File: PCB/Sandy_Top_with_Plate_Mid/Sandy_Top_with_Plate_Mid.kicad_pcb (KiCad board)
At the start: 2 copper layers, 285 x 75.1 mm, 63 parts, among them J1 Conn_02x02_Top_Bottom, J2 Conn_02x02_Top_Bottom, J3 Conn_02x02_Top_Bottom

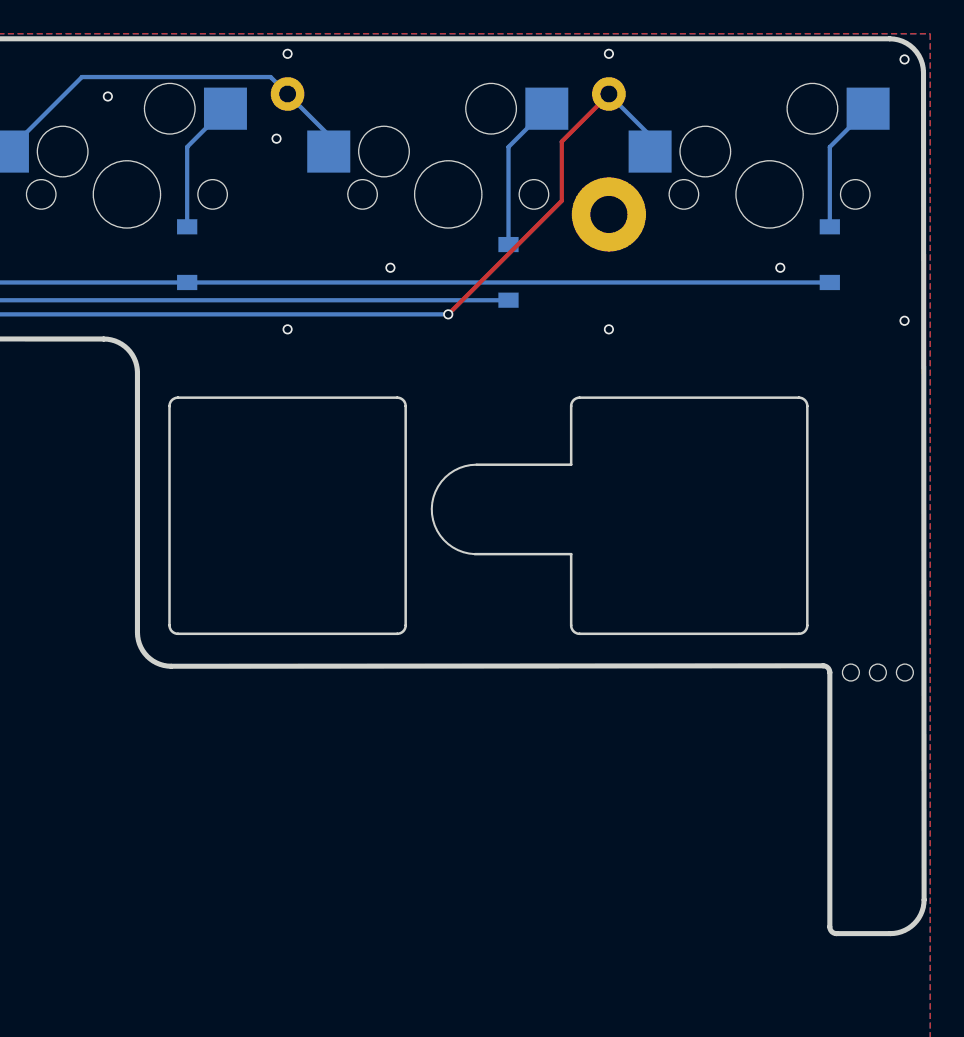
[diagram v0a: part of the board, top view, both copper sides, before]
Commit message: バージョン表記部分にプレートである旨を追記
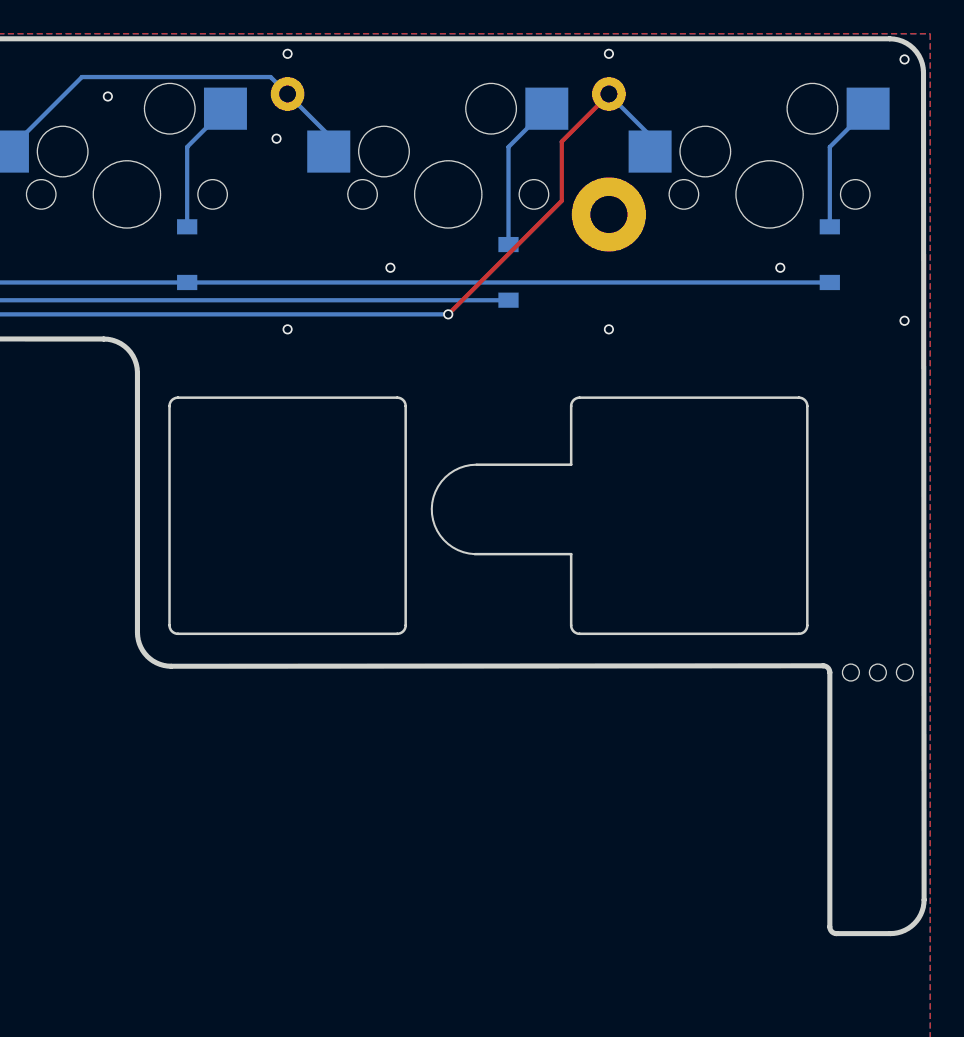
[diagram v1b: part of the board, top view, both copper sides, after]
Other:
- board text added: "#Sandy_kbd v.0.2 Top & Mid plate by @jpskenn"
- board text removed: "#Sandy_kbd v.0.2, Top by @jpskenn"
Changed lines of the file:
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@@
     (fp_arc (start -118.325 -37.80004) (mid -118.678553 -37.946487) (end -118.825 -38.30004)
       (stroke (width 0.1) (type solid)) (layer "Dwgs.User"))
-    (fp_arc (start 114.175 -9.90004) (mid 114.731476 -11.243582) (end 116.075 -11.80004)
+    (fp_arc (start 114.175 -9.90004) (mid 114.731482 -11.243546) (end 116.075 -11.80004)
       (stroke (width 0.12) (type solid)) (layer "Dwgs.User"))
-    (fp_arc (start 114.923491 -9.898554) (mid 115.274975 -10.747086) (end 116.123491 -11.098554)
+    (fp_arc (start 114.923491 -9.898554) (mid 115.274981 -10.74705) (end 116.123491 -11.098554)
       (stroke (width 0.12) (type solid)) (layer "Dwgs.User"))
-    (fp_arc (start 116.075 -8.00004) (mid 114.731482 -8.55651) (end 114.175 -9.90004)
+    (fp_arc (start 116.075 -8.00004) (mid 114.731447 -8.556504) (end 114.175 -9.90004)
       (stroke (width 0.12) (type solid)) (layer "Dwgs.User"))
-    (fp_arc (start 116.123491 -8.698554) (mid 115.274982 -9.050056) (end 114.923491 -9.898554)
+    (fp_arc (start 116.123491 -8.698554) (mid 115.275017 -9.050062) (end 114.923491 -9.898554)
       (stroke (width 0.12) (type solid)) (layer "Dwgs.User"))
-    (fp_arc (start 118.923491 -11.098554) (mid 119.772038 -10.747112) (end 120.123491 -9.898554)
+    (fp_arc (start 118.923491 -11.098554) (mid 119.772073 -10.747118) (end 120.123491 -9.898554)
       (stroke (width 0.12) (type solid)) (layer "Dwgs.User"))
-    (fp_arc (start 118.975 -11.80004) (mid 120.318488 -11.243516) (end 120.875 -9.90004)
+    (fp_arc (start 118.975 -11.80004) (mid 120.318452 -11.24351) (end 120.875 -9.90004)
       (stroke (width 0.12) (type solid)) (layer "Dwgs.User"))
-    (fp_arc (start 120.123491 -9.898554) (mid 119.772032 -9.050029) (end 118.923491 -8.698554)
+    (fp_arc (start 120.123491 -9.898554) (mid 119.772038 -9.049994) (end 118.923491 -8.698554)
       (stroke (width 0.12) (type solid)) (layer "Dwgs.User"))
-    (fp_arc (start 120.875 -9.90004) (mid 120.318482 -8.556576) (end 118.975 -8.00004)
+    (fp_arc (start 120.875 -9.90004) (mid 120.318488 -8.556541) (end 118.975 -8.00004)
       (stroke (width 0.12) (type solid)) (layer "Dwgs.User"))
     (fp_circle (center -117.325 -9.90004) (end -116.025 -9.90004)
@@
     (fp_arc (start 27.975 20.214174) (mid 28.560766 18.799948) (end 29.975 18.214174)
       (stroke (width 0.3) (type solid)) (layer "Edge.Cuts"))
-    (fp_arc (start 27.975 35.345746) (mid 27.389238 36.759982) (end 25.975 37.345746)
+    (fp_arc (start 27.975 35.345746) (mid 27.389238 36.759986) (end 25.975 37.345746)
       (stroke (width 0.3) (type solid)) (layer "Edge.Cuts"))
     (fp_arc (start 35.075 2.525) (mid 35.428553 2.671447) (end 35.575 3.025)
@@
     (fp_arc (start 56.555 -2.937398) (mid 55.969213 -1.523186) (end 54.555 -0.937398)
       (stroke (width 0.3) (type solid)) (layer "Edge.Cuts"))
-    (fp_arc (start 93.875 -20.001612) (mid 95.289212 -19.41585) (end 95.875 -18.001612)
+    (fp_arc (start 93.875 -20.001612) (mid 95.289182 -19.41582) (end 95.875 -18.001612)
       (stroke (width 0.3) (type solid)) (layer "Edge.Cuts"))
     (fp_arc (start 97.775 -16.025) (mid 97.921447 -16.378553) (end 98.275 -16.525)
       (stroke (width 0.15) (type solid)) (layer "Edge.Cuts"))
-    (fp_arc (start 97.875 -0.60004) (mid 96.460771 -1.1858) (end 95.875 -2.60004)
+    (fp_arc (start 97.875 -0.60004) (mid 96.460736 -1.185794) (end 95.875 -2.60004)
       (stroke (width 0.3) (type solid)) (layer "Edge.Cuts"))
     (fp_arc (start 98.275 -2.525) (mid 97.921447 -2.671447) (end 97.775 -3.025)
@@
     (fp_arc (start 136.521875 -0.628468) (mid 136.804693 -0.511288) (end 136.921875 -0.228468)
       (stroke (width 0.3) (type solid)) (layer "Edge.Cuts"))
-    (fp_arc (start 137.321875 15.249657) (mid 137.039034 15.132518) (end 136.921875 14.849657)
+    (fp_arc (start 137.321875 15.249657) (mid 137.038999 15.132524) (end 136.921875 14.849657)
       (stroke (width 0.3) (type solid)) (layer "Edge.Cuts"))
-    (fp_arc (start 140.475 -37.80004) (mid 141.889198 -37.214227) (end 142.475 -35.80004)
+    (fp_arc (start 140.475 -37.80004) (mid 141.889163 -37.214221) (end 142.475 -35.80004)
       (stroke (width 0.3) (type solid)) (layer "Edge.Cuts"))
     (fp_arc (start 142.510786 13.249657) (mid 141.925014 14.663893) (end 140.510786 15.249657)
@@
     (effects (font (size 2.5 2.5) (thickness 0.4) italic) (justify mirror))
   )
-  (gr_text "#Sandy_kbd v.0.2, Top\nby @jpskenn" (at 169 51.7) (layer "B.SilkS")
+  (gr_text "#Sandy_kbd v.0.2\nTop & Mid plate\nby @jpskenn" (at 166.314685 53.197155) (layer "B.SilkS")
     (effects (font (size 1.6 1.6) (thickness 0.15)) (justify left mirror))
   )

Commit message: Top基板（Midプレート付き）からディフューザーを削除
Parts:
- REF**: footprint locallib:60_Outline-Sandy-Top2-with-Mid-plate-from-Mid4 -> locallib:60_Outline-Sandy-Top3-with-Mid-plate-from-Mid4
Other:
- outline, holes or cut-outs redrawn

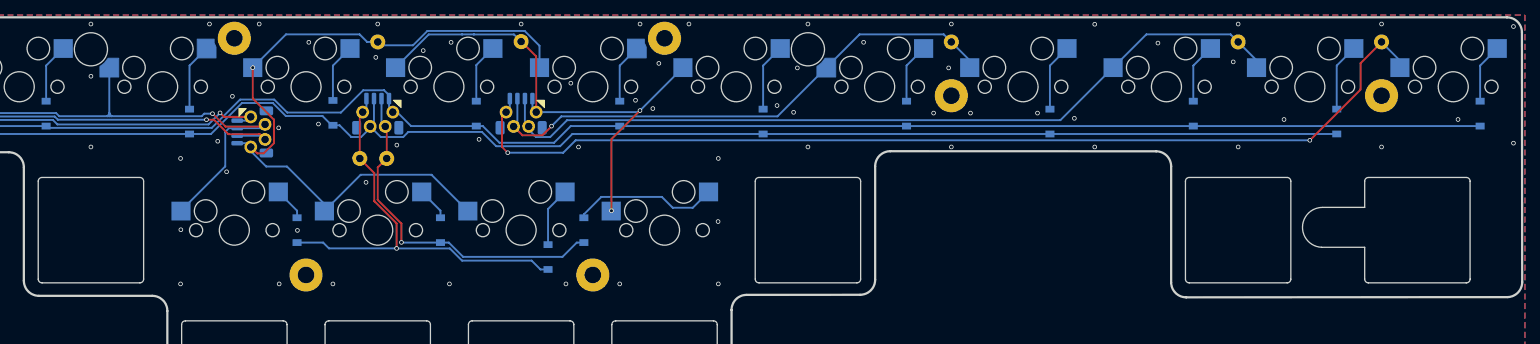
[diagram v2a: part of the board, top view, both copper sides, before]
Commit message: ソケットに近いSHコネクタ2個を少し後ろに下げ、ケーブルを抜き差ししやすくした
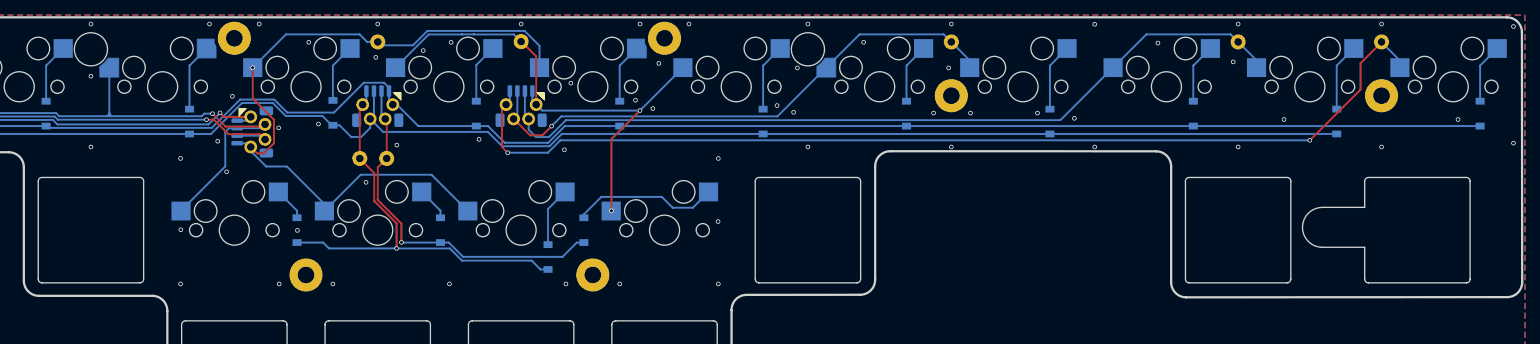
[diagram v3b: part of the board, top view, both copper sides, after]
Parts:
- moved J1 1.00 mm to (167.5, 29.6)
- moved J2 1.00 mm to (148.5, 29.6)
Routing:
- net Top_row0: track 276.6 -> 278.0 mm
- net Top_row6: track 57.1 -> 58.1 mm
- net Top_row1: track 47.0 -> 48.0 mm
- net Top_col7: track 136.6 -> 137.6 mm
- net Top_col6: track 109.5 -> 110.5 mm
- net Top_row5: track 244.0 -> 244.9 mm
- net Top_col4: track 68.0 -> 67.2 mm

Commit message: バージョン表記調整
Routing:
- net Top_row5: track 244.9 -> 242.4 mm
- net Top_col7: track 137.6 -> 135.5 mm
- net Top_row0: track 278.0 -> 276.9 mm
- net Top_col6: track 110.5 -> 109.6 mm
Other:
- board text added: "#Sandy_kbd v.0.2, Top & Plate for Mid by @jpskenn"
- board text removed: "#Sandy_kbd v.0.2 Top & Mid plate by @jpskenn"
